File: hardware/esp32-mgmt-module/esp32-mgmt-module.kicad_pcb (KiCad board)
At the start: 4 copper layers, 77 x 31.8 mm, 91 parts, among them J1 Bus_PCI_Express_x1, J2 BOOT, J3 RJ45_Hanrun_HR913550A_Horizon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, J4 GPIO, J5 SWD, J6 USB_C, J7 UART, Q1 MMBT3904, Q2 MMBT3904, SW1 RESET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

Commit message: chore: add component placement corrections
chore: rotate uart header so ground is pin 1
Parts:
- moved J7 5.10 mm to (95.4, 33.7), turned to -90 degrees
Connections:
- J7 pad 1: /RXD_OUT -> GND
- J7 pad 3: GND -> /RXD_OUT

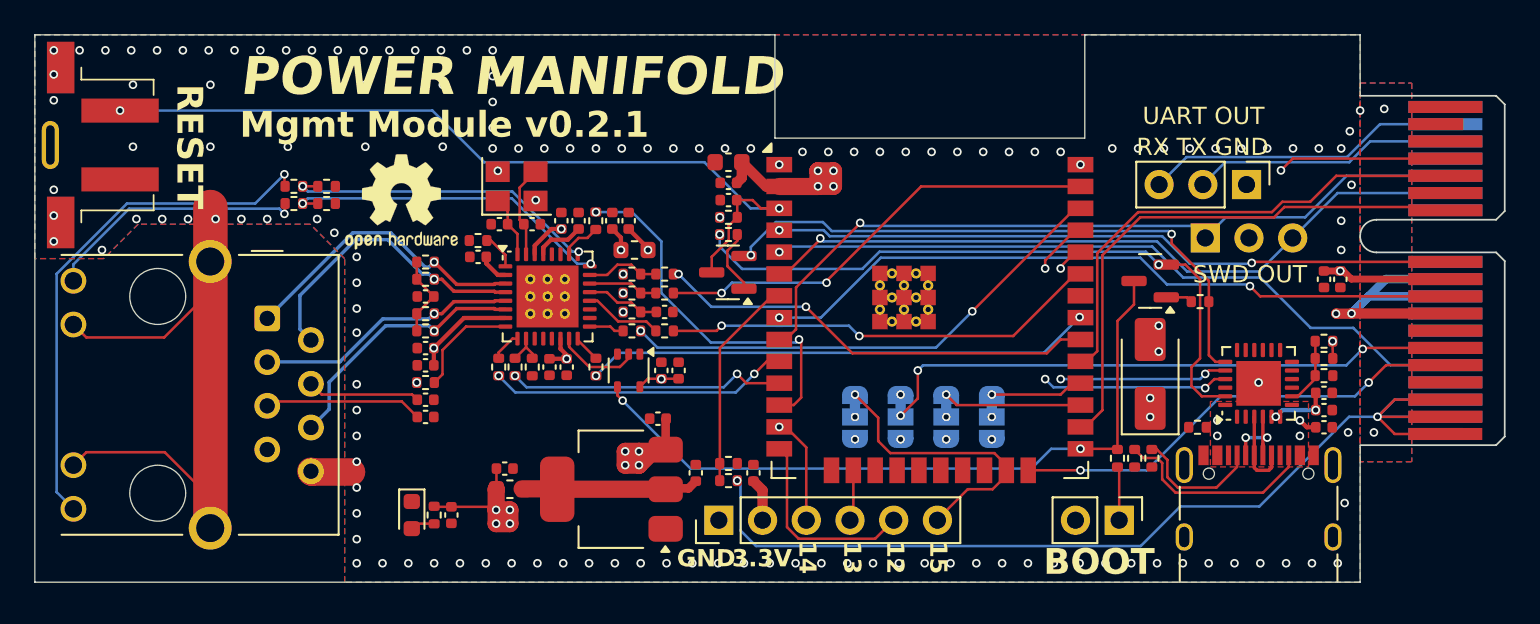
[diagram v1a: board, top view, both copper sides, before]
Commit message: fix: remove need for via-in-pad
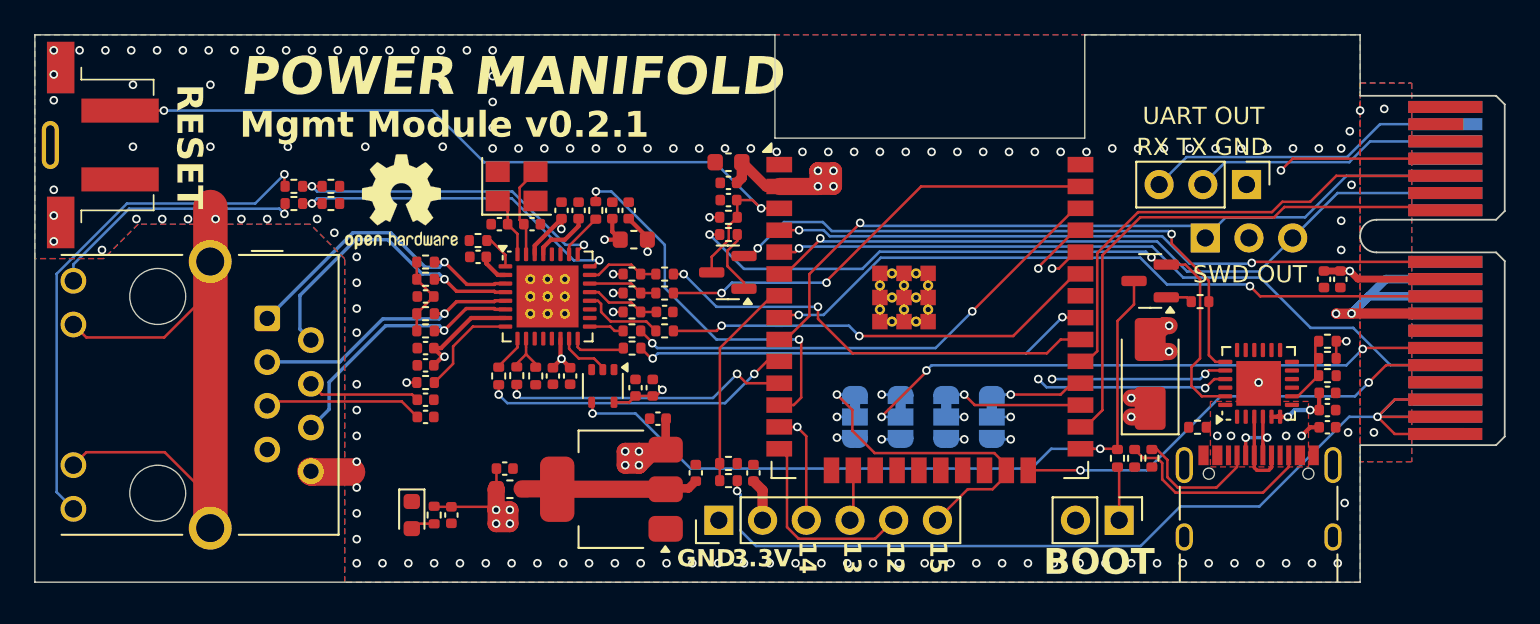
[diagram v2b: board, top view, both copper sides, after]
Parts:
- moved R5 2.37 mm to (59.7, 43.2), turned to 180 degrees
- moved C14 1.80 mm to (59.9, 45.5)
- moved C16 1.80 mm to (60.9, 45.5)
- moved U2 1.75 mm to (58.0, 45.4)
- moved L1 0.60 mm to (59.8, 36.9)
- moved C17 0.60 mm to (55.6, 35.2)
- moved C21 0.60 mm to (58.5, 35.2)
- moved C5 0.60 mm to (56.6, 35.2)
- moved C9 0.60 mm to (59.5, 35.2)
- moved R10 0.60 mm to (57.6, 35.2)
- moved C10 0.56 mm to (55.1, 44.8)
- moved C8 0.56 mm to (56.1, 44.8)
- moved R1 0.56 mm to (54.1, 44.8)
- moved R8 0.52 mm to (52.0, 44.8)
- moved R9 0.51 mm to (53.0, 44.8)
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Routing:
- net +3.3V: track 35.4 -> 40.0 mm
- net +5V: track 21.5 -> 25.0 mm
- net /RXD2: track 14.4 -> 17.6 mm
- net /TXD2: track 12.0 -> 15.1 mm
- net /EMAC_TXD0: track 29.6 -> 26.8 mm
- net /REF_CLK_MCU: track 42.0 -> 44.3 mm
- net /SW_A2: track 43.6 -> 45.7 mm
- net /GPIO15: track 17.0 -> 19.0 mm
- net /REF_CLK_ETH: track 4.87 -> 3.13 mm
- net Net-(U1-TXD[0]): track 1.58 -> 3.25 mm
- net Net-(D1-K): track 45.6 -> 47.1 mm
- net /TXD_OUT: track 37.2 -> 38.7 mm
- net /SW_A1: track 34.2 -> 35.6 mm
- net /RXD0: track 26.6 -> 27.9 mm
- net /~{RESET}: track 48.1 -> 47.1 mm
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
